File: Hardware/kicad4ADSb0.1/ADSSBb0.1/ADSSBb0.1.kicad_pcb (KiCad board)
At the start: 2 copper layers, 43.7 x 27.4 mm, 19 parts, among them IC1 AD7856ANZ, J1 ICSP ARDUINO NANO, J2 Conn_01x04, J3 Conn_01x04, J4 Conn_01x04, J5 Conn_01x04, J6 Conn_01x04, J7 Conn_01x04, J8 Conn_01x03, U1 MAX7375AXR405

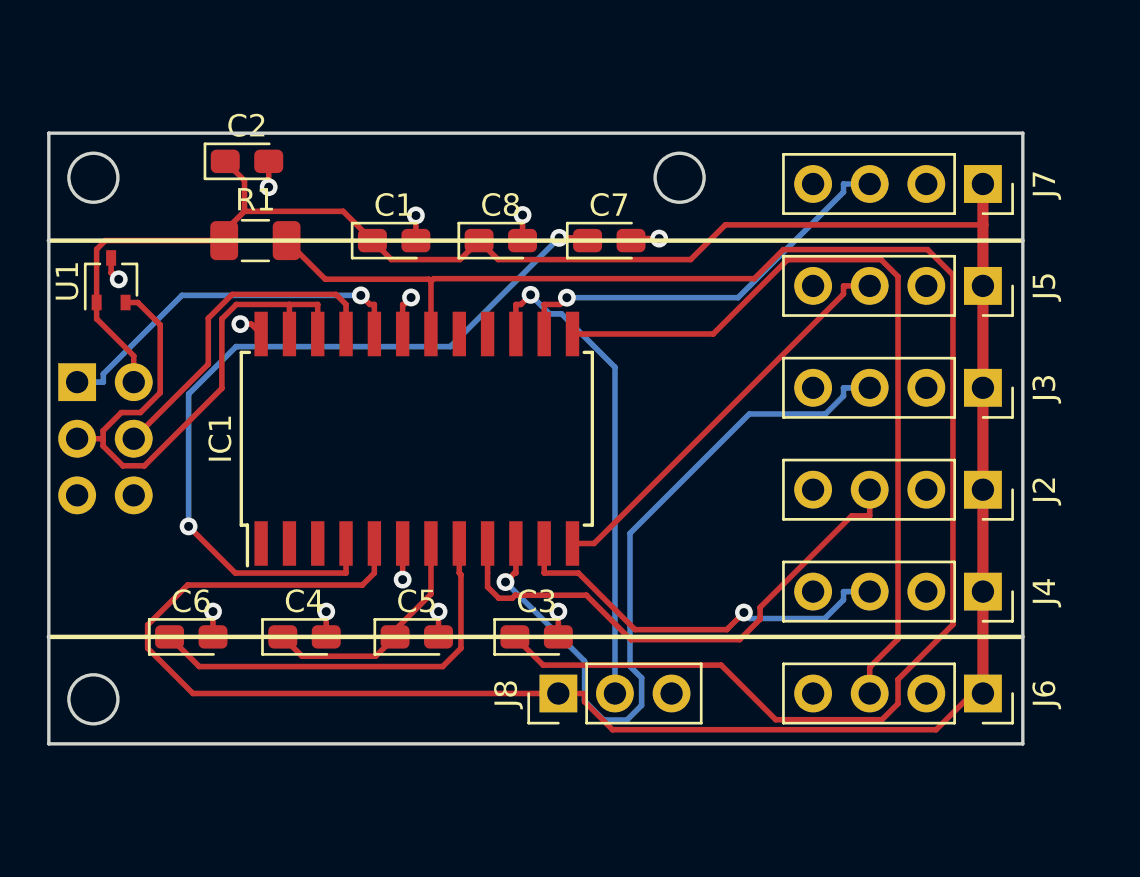
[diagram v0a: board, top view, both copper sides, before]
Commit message: SIL moved
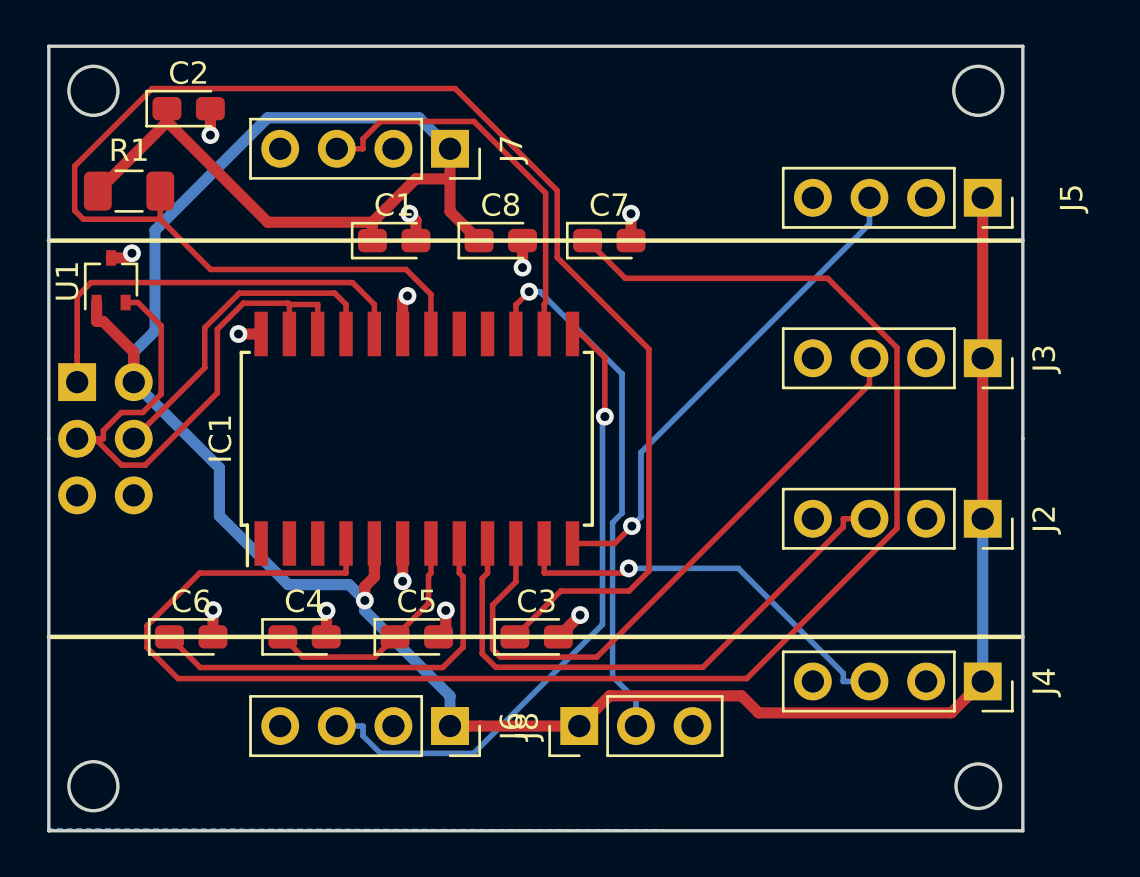
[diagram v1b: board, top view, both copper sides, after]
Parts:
- moved J7 24.0 mm to (132.3, 105.1)
- moved J6 24.0 mm to (132.3, 131.0)
- moved R1 6.09 mm to (117.9, 107.0)
- moved J4 4.03 mm to (156.2, 129.0)
- moved J5 3.95 mm to (156.2, 107.3)
- moved C2 3.53 mm to (120.6, 103.3)
- moved J8 1.74 mm to (138.1, 131.0)
- moved J3 1.32 mm to (156.2, 114.5)
- moved J2 1.30 mm to (156.2, 121.7)
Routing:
- net Net-(C7-Pad1): track 36.0 -> 73.2 mm, vias 2 -> 0
- net Net-(IC1-Pad13): track 35.5 -> 29.0 mm, vias 0 -> 1
- net Net-(IC1-Pad10): track 33.6 -> 28.5 mm, vias 1 -> 0
- net Net-(IC1-Pad12): track 18.3 -> 22.1 mm, vias 0 -> 1
- net /5V: track 128.6 -> 126.1 mm, vias 0 -> 1
- net /MISO: track 16.7 -> 19.2 mm, vias 1 -> 0
- net Net-(IC1-Pad15): track 21.9 -> 24.3 mm
- net Net-(IC1-Pad9): track 24.0 -> 25.6 mm
- net GND: track 15.0 -> 15.6 mm
- net Net-(IC1-Pad14): track 18.4 -> 17.8 mm, vias 1 -> 0
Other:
- board size 43.7 x 27.4 mm -> 43.7 x 35.2 mm
